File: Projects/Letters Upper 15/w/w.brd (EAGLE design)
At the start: 16.5 x 21.6 mm, 37 parts

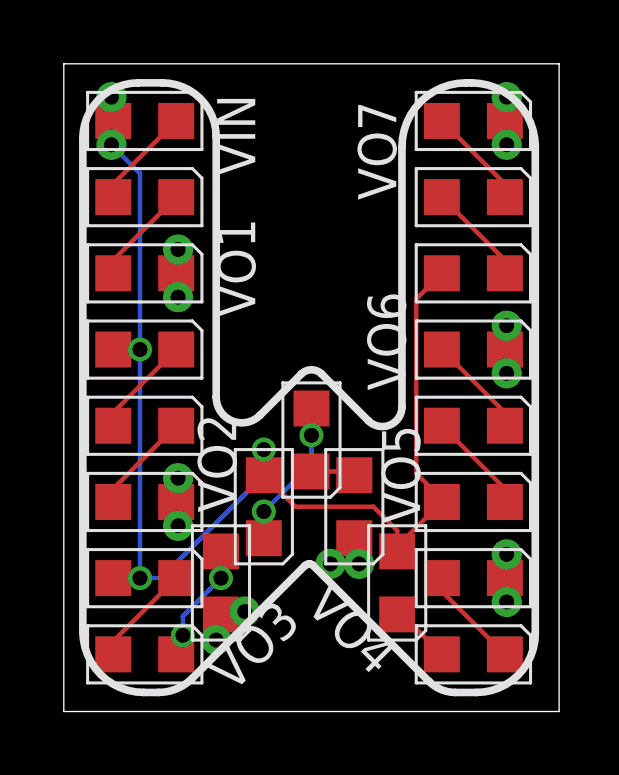
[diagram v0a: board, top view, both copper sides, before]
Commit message: 
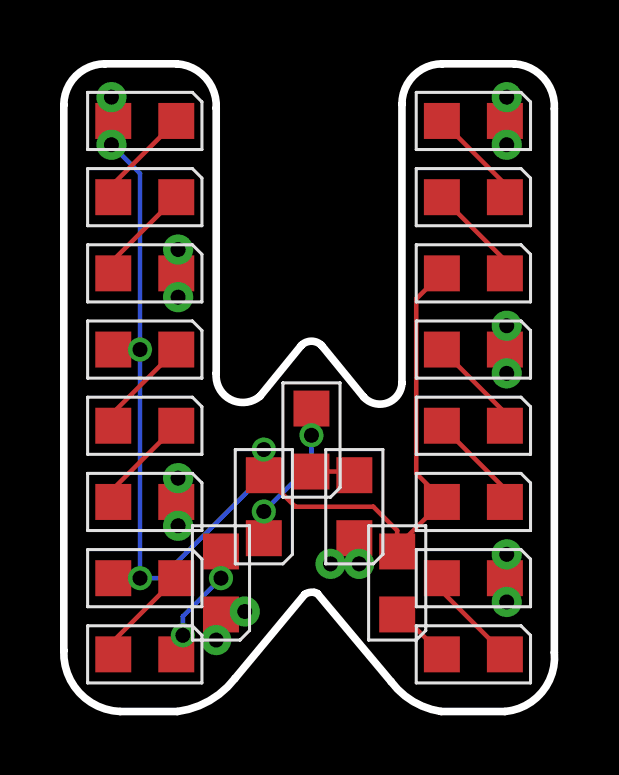
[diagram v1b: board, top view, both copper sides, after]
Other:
- board size 16.5 x 21.6 mm -> 16.4 x 21.6 mm
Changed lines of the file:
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@@
 <layer number="18" name="Vias" color="2" fill="1" visible="yes" active="yes"/>
 <layer number="19" name="Unrouted" color="6" fill="1" visible="yes" active="yes"/>
-<layer number="20" name="Dimension" color="15" fill="1" visible="yes" active="yes"/>
+<layer number="20" name="Dimension" color="3" fill="1" visible="yes" active="yes"/>
 <layer number="21" name="tPlace" color="7" fill="1" visible="yes" active="yes"/>
 <layer number="22" name="bPlace" color="7" fill="1" visible="yes" active="yes"/>
@@
 <layer number="24" name="bOrigins" color="15" fill="1" visible="yes" active="yes"/>
 <layer number="25" name="tNames" color="7" fill="1" visible="yes" active="yes"/>
-<layer number="26" name="bNames" color="7" fill="1" visible="yes" active="yes"/>
+<layer number="26" name="bNames" color="5" fill="1" visible="yes" active="yes"/>
 <layer number="27" name="tValues" color="7" fill="1" visible="yes" active="yes"/>
 <layer number="28" name="bValues" color="7" fill="1" visible="yes" active="yes"/>
@@
 <board>
 <plain>
-<wire x1="0" y1="0" x2="16.51" y2="0" width="0" layer="20"/>
-<wire x1="16.51" y1="0" x2="16.51" y2="21.59" width="0" layer="20"/>
-<wire x1="16.51" y1="21.59" x2="0" y2="21.59" width="0" layer="20"/>
-<wire x1="0" y1="21.59" x2="0" y2="0" width="0" layer="20"/>
 <text x="0.635" y="0.635" size="20.32" layer="201" font="fixed" ratio="22" distance="27">W</text>
-<wire x1="2.486325" y1="20.955" x2="3.28395" y2="20.955" width="0.254" layer="21"/>
-<wire x1="3.28395" y1="20.955" x2="5.08" y2="19.15895" width="0.254" layer="21" curve="-90"/>
-<wire x1="5.08" y1="19.15895" x2="5.08" y2="10.477646875" width="0.254" layer="21"/>
-<wire x1="5.08" y1="10.477646875" x2="6.53939375" y2="9.87314375" width="0.254" layer="21" curve="134.999852"/>
-<wire x1="6.53939375" y1="9.87314375" x2="7.918240625" y2="11.251990625" width="0.254" layer="21"/>
-<wire x1="7.918240625" y1="11.251990625" x2="8.591759375" y2="11.251990625" width="0.254" layer="21" curve="-90"/>
-<wire x1="8.591759375" y1="11.251990625" x2="10.153878125" y2="9.689871875" width="0.254" layer="21"/>
-<wire x1="2.486325" y1="20.955" x2="0.635" y2="19.103675" width="0.254" layer="21" curve="90"/>
-<wire x1="0.635" y1="19.103675" x2="0.635" y2="2.667990625" width="0.254" layer="21"/>
-<wire x1="0.635" y1="2.667990625" x2="2.667990625" y2="0.635" width="0.254" layer="21" curve="90"/>
-<wire x1="2.667990625" y1="0.635" x2="3.1524375" y2="0.635" width="0.254" layer="21"/>
-<wire x1="3.1524375" y1="0.635" x2="4.27496875" y2="1.09996875" width="0.254" layer="21" curve="45"/>
-<wire x1="4.27496875" y1="1.09996875" x2="8.03049375" y2="4.85549375" width="0.254" layer="21"/>
-<wire x1="8.03049375" y1="4.85549375" x2="8.18924375" y2="4.92125" width="0.254" layer="21" curve="-45"/>
-<wire x1="8.18924375" y1="4.92125" x2="8.301496875" y2="4.874753125" width="0.254" layer="21" curve="-45"/>
-<wire x1="8.301496875" y1="4.874753125" x2="12.1781" y2="0.99815" width="0.254" layer="21"/>
-<wire x1="12.1781" y1="0.99815" x2="13.054821875" y2="0.635" width="0.254" layer="21" curve="44.999856"/>
-<wire x1="13.054821875" y1="0.635" x2="13.752621875" y2="0.635" width="0.254" layer="21"/>
-<wire x1="13.752621875" y1="0.635" x2="15.71625" y2="2.598628125" width="0.254" layer="21" curve="90"/>
-<wire x1="15.71625" y1="2.598628125" x2="15.71625" y2="18.8192375" width="0.254" layer="21"/>
-<wire x1="15.71625" y1="18.8192375" x2="13.5804875" y2="20.955" width="0.254" layer="21" curve="90"/>
-<wire x1="13.5804875" y1="20.955" x2="13.4070125" y2="20.955" width="0.254" layer="21"/>
-<wire x1="13.4070125" y1="20.955" x2="11.27125" y2="18.8192375" width="0.254" layer="21" curve="90"/>
-<wire x1="10.153878125" y1="9.689871875" x2="11.27125" y2="10.1527" width="0.254" layer="21" curve="134.999726"/>
-<wire x1="11.27125" y1="10.1527" x2="11.27125" y2="18.8192375" width="0.254" layer="21"/>
+<wire x1="1.375075" y1="21.59" x2="3.7602" y2="21.59" width="0.254" layer="20"/>
+<wire x1="3.7602" y1="21.59" x2="5.08" y2="20.11145" width="0.254" layer="20" curve="-90"/>
+<wire x1="5.08" y1="20.11145" x2="5.08" y2="11.271396875" width="0.254" layer="20"/>
+<wire x1="5.08" y1="11.271396875" x2="6.53939375" y2="10.50814375" width="0.254" layer="20" curve="134.999852"/>
+<wire x1="6.53939375" y1="10.50814375" x2="7.918240625" y2="12.204490625" width="0.254" layer="20"/>
+<wire x1="7.918240625" y1="12.204490625" x2="8.591759375" y2="12.204490625" width="0.254" layer="20" curve="-90"/>
+<wire x1="8.591759375" y1="12.204490625" x2="9.995128125" y2="10.483621875" width="0.254" layer="20"/>
+<wire x1="1.375075" y1="21.59" x2="0" y2="20.214925" width="0.254" layer="20" curve="90"/>
+<wire x1="0" y1="20.214925" x2="0" y2="2.032990625" width="0.254" layer="20"/>
+<wire x1="0" y1="2.032990625" x2="1.874240625" y2="0" width="0.254" layer="20" curve="90"/>
+<wire x1="1.874240625" y1="0" x2="3.7874375" y2="0" width="0.254" layer="20"/>
+<wire x1="3.7874375" y1="0" x2="5.70371875" y2="1.09996875" width="0.254" layer="20" curve="45"/>
+<wire x1="5.70371875" y1="1.09996875" x2="8.03049375" y2="3.90299375" width="0.254" layer="20"/>
+<wire x1="8.03049375" y1="3.90299375" x2="8.34799375" y2="3.96875" width="0.254" layer="20" curve="-45"/>
+<wire x1="8.34799375" y1="3.96875" x2="8.460246875" y2="3.922253125" width="0.254" layer="20" curve="-45"/>
+<wire x1="8.460246875" y1="3.922253125" x2="10.9081" y2="0.99815" width="0.254" layer="20"/>
+<wire x1="10.9081" y1="0.99815" x2="12.578571875" y2="0" width="0.254" layer="20" curve="45"/>
+<wire x1="12.578571875" y1="0" x2="14.705121875" y2="0" width="0.254" layer="20"/>
+<wire x1="14.705121875" y1="0" x2="16.35125" y2="1.963628125" width="0.254" layer="20" curve="90"/>
+<wire x1="16.35125" y1="1.963628125" x2="16.35125" y2="20.0892375" width="0.254" layer="20"/>
+<wire x1="16.35125" y1="20.0892375" x2="15.0092375" y2="21.59" width="0.254" layer="20" curve="90"/>
+<wire x1="15.0092375" y1="21.59" x2="12.6132625" y2="21.59" width="0.254" layer="20"/>
+<wire x1="12.6132625" y1="21.59" x2="11.27125" y2="20.2479875" width="0.254" layer="20" curve="90"/>
+<wire x1="9.995128125" y1="10.483621875" x2="11.27125" y2="10.94645" width="0.254" layer="20" curve="134.999726"/>
+<wire x1="11.27125" y1="10.94645" x2="11.27125" y2="20.2479875" width="0.254" layer="20"/>
 </plain>
 <attributes>
@@
 </element>
 <element name="VIN" library="CyberRailGuru" package="P1-20" value="" x="1.5875" y="18.89125" smashed="yes">
-<attribute name="NAME" x="5.11175" y="20.574" size="1.27" layer="25" ratio="15" rot="R270"/>
+<attribute name="NAME" x="3.4925" y="18.0975" size="1.27" layer="26" ratio="15" rot="R90"/>
 <attribute name="VALUE" x="0.0635" y="16.85925" size="1.27" layer="27" ratio="10"/>
 </element>
 <element name="VO1" library="CyberRailGuru" package="P1-20" value="" x="3.81" y="13.81125" smashed="yes">
-<attribute name="NAME" x="5.11175" y="16.4465" size="1.27" layer="25" ratio="15" rot="R270"/>
+<attribute name="NAME" x="3.175" y="13.0175" size="1.27" layer="26" ratio="15" rot="R90"/>
 <attribute name="VALUE" x="2.286" y="11.77925" size="1.27" layer="27" ratio="10"/>
 </element>
 <element name="VO2" library="CyberRailGuru" package="P1-20" value="" x="3.81" y="6.19125" smashed="yes">
-<attribute name="NAME" x="4.47675" y="9.93775" size="1.27" layer="25" ratio="15" rot="R270"/>
+<attribute name="NAME" x="3.175" y="5.3975" size="1.27" layer="26" ratio="15" rot="R90"/>
 <attribute name="VALUE" x="2.286" y="4.15925" size="1.27" layer="27" ratio="10"/>
 </element>
 <element name="VO3" library="CyberRailGuru" package="P1-20" value="" x="5.08" y="2.38125" smashed="yes">
-<attribute name="NAME" x="5.625196875" y="0.590096875" size="1.27" layer="25" ratio="15" rot="R45"/>
+<attribute name="NAME" x="4.1275" y="2.2225" size="1.27" layer="26" ratio="15" rot="R45"/>
 <attribute name="VALUE" x="3.556" y="0.34925" size="1.27" layer="27" ratio="10"/>
 </element>
 <element name="VO4" library="CyberRailGuru" package="P1-20" value="" x="8.89" y="4.92125" smashed="yes">
-<attribute name="NAME" x="8.004853125" y="3.47005" size="1.27" layer="25" ratio="15" rot="R315"/>
+<attribute name="NAME" x="7.9375" y="5.715" size="1.27" layer="26" ratio="15"/>
 <attribute name="VALUE" x="7.366" y="2.88925" size="1.27" layer="27" ratio="10"/>
 </element>
 <element name="VO5" library="CyberRailGuru" package="P1-20" value="" x="14.76375" y="3.65125" smashed="yes">
-<attribute name="NAME" x="11.8745" y="6.25475" size="1.27" layer="25" ratio="15" rot="R90"/>
+<attribute name="NAME" x="13.97" y="2.8575" size="1.27" layer="26" ratio="15" rot="R90"/>
 <attribute name="VALUE" x="13.23975" y="1.61925" size="1.27" layer="27" ratio="10"/>
 </element>
 <element name="VO6" library="CyberRailGuru" package="P1-20" value="" x="14.76375" y="11.27125" smashed="yes">
-<attribute name="NAME" x="11.39825" y="10.69975" size="1.27" layer="25" ratio="15" rot="R90"/>
+<attribute name="NAME" x="13.97" y="10.4775" size="1.27" layer="26" ratio="15" rot="R90"/>
 <attribute name="VALUE" x="13.23975" y="9.23925" size="1.27" layer="27" ratio="10"/>
 </element>
@@
 </element>
 <element name="VO7" library="CyberRailGuru" package="P1-20" value="" x="14.76375" y="18.89125" smashed="yes">
-<attribute name="NAME" x="11.08075" y="17.04975" size="1.27" layer="25" ratio="15" rot="R90"/>
+<attribute name="NAME" x="13.97" y="17.78" size="1.27" layer="26" ratio="15" rot="R90"/>
 <attribute name="VALUE" x="13.23975" y="16.85925" size="1.27" layer="27" ratio="10"/>
 </element>
